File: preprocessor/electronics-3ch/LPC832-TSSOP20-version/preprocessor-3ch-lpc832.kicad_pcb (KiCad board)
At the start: 2 copper layers, 17 x 17 mm, 11 parts, among them P1 ST-IN, P2 ST-OUT, P3 TH-IN, P4 TH-OUT, P5 AUX-IN, P6 LIGHT CONTROLLER, U1 MCP1703T-3302E/CB, U2 LPC832M101FDH20

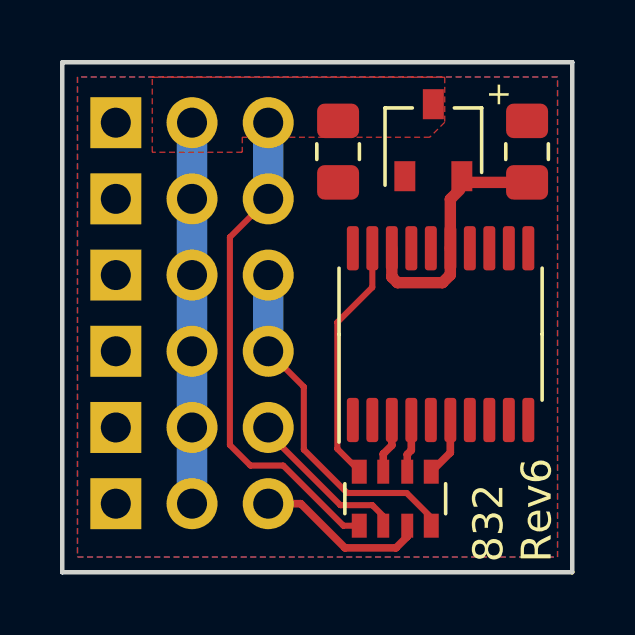
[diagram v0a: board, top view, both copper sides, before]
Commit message: Make ground flood go underneath LPC832
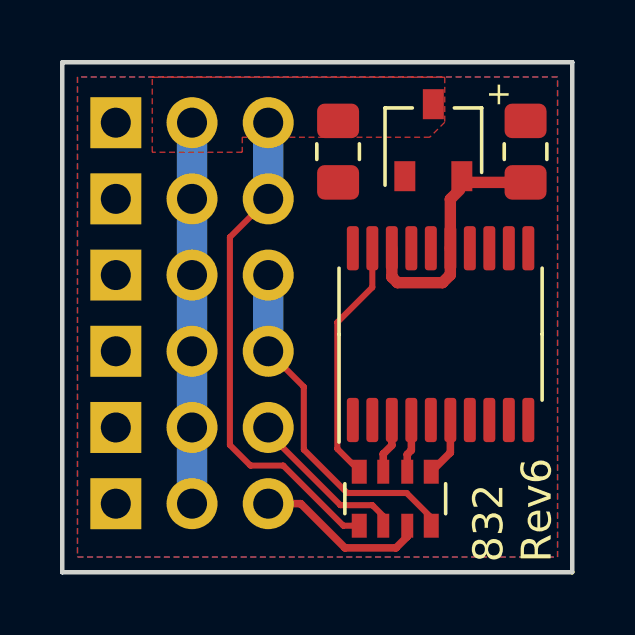
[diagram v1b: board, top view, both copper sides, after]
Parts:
- moved C2 0.05 mm to (129.7, 52.0)

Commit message: Add Gerber for LPC832 variants
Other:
- rule pad_to_mask_clearance: 0.0508 -> 0
